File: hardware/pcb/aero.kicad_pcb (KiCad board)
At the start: 4 copper layers, 41 x 50 mm, 310 parts, among them CON1 USB-MICRO-B, CON2 MMCX_CONN, J1 CORTEX_DBG_CONN, J2 LiPoly_Conn, Q1 BSS138, SW1 SW_PUSH, U1 STM32L151C8, U10 BU4SU69G2, U11 BU4SU69G2, U12 NC7WZ17, U13 u-blox_max-7c/q, U14 MAX2659, U2 nRF8001, U3 2450BM14A0002, U4 ms5611, U5 BMX055, U6 AT45DB321E, U7 BQ24040DSQ, U8 TPS783, U9 TPS61041, Y1 Crystal, Y2 32.768KHz, Y3 16MHz

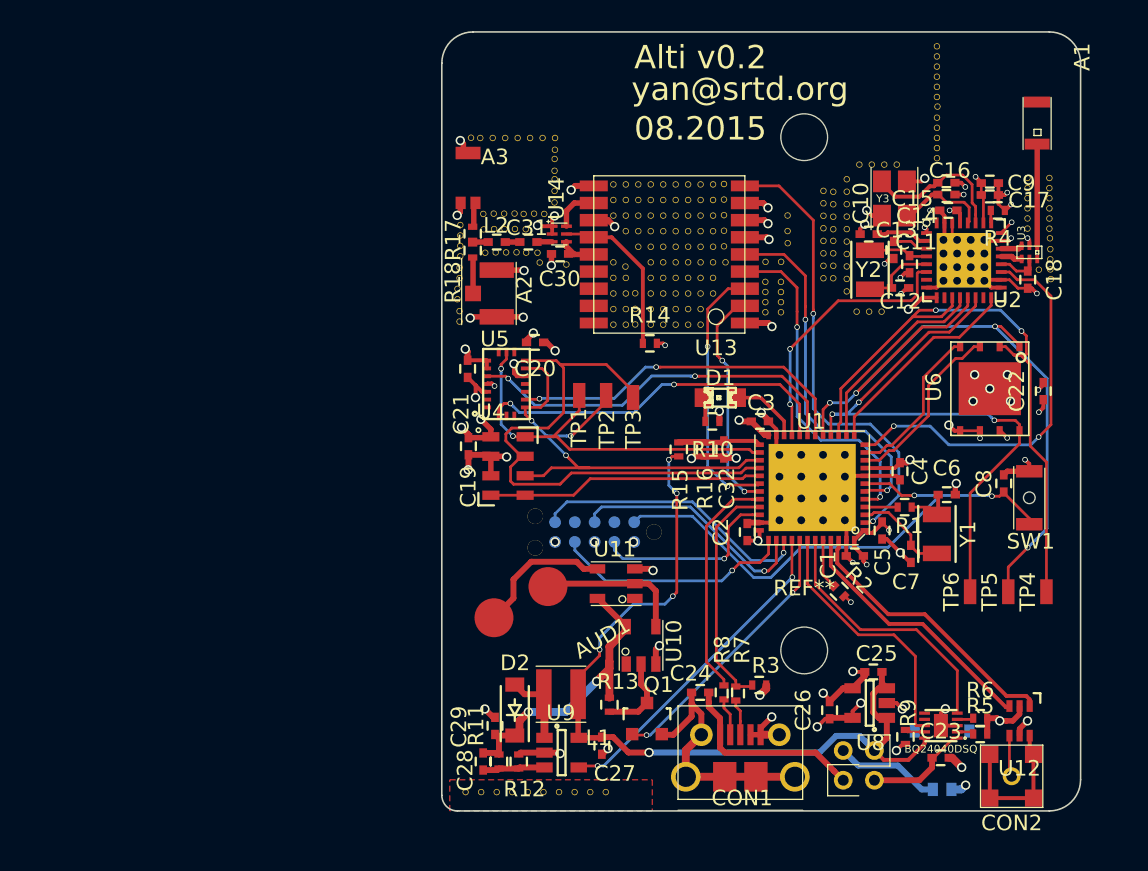
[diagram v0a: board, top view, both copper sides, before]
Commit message: moved balun further from nrf8001
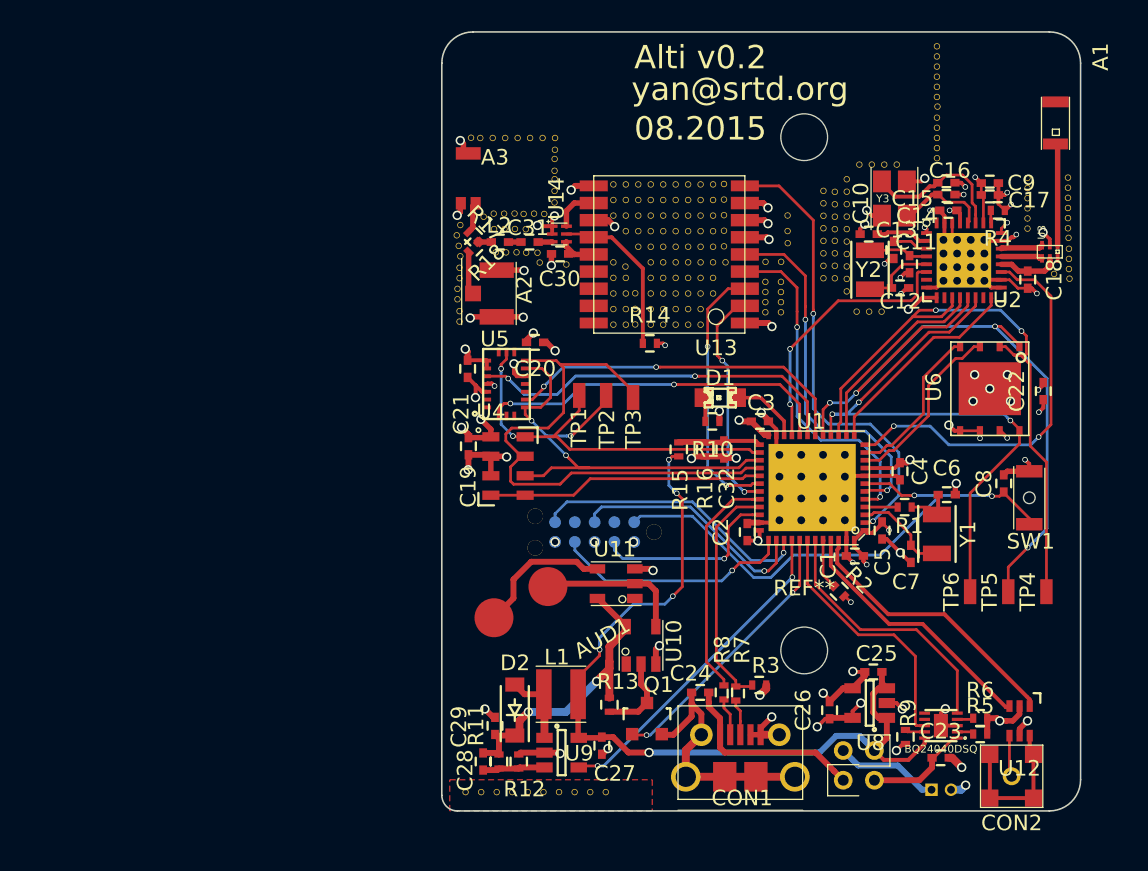
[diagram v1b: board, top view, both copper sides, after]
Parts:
- removed the REF**1111 at (127.8, 79.2)
- removed the REF**1111 at (127.7, 77.7)
- J2: footprint aero:Conn_Molex_78171-02 -> Connectors_Molex:Connector_Molex_PicoBlade_53048-0210
- moved U3 1.31 mm to (164.0, 79.1)
- moved REF**11611 1.19 mm to (165.2, 77.6)
- moved REF**11612 1.19 mm to (165.3, 79.6)
- moved REF**11613 1.19 mm to (165.3, 78.9)
- moved REF**11613 1.19 mm to (165.2, 76.3)
- moved REF**11615 1.19 mm to (165.2, 75.0)
- moved REF**11616 1.19 mm to (165.2, 74.4)
- moved REF**11611 1.19 mm to (165.3, 80.2)
- moved REF**11612 1.19 mm to (165.2, 77.0)
- moved REF**11614 1.19 mm to (165.2, 75.7)
- moved REF**11616 1.19 mm to (165.3, 80.8)
- moved REF**11616 1.19 mm to (165.2, 78.2)
- moved A1 1.18 mm to (164.4, 70.8)
- moved REF**11611 1.01 mm to (164.3, 80.5)
- moved J2 0.68 mm to (156.4, 113.6)
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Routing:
- net Net-(C18-Pad1): track 2.70 -> 4.07 mm
- net Net-(U2-Pad22): track 1.38 -> 2.71 mm
- net Net-(U2-Pad21): track 1.37 -> 2.66 mm
- net GND: track 126.0 -> 126.9 mm
- net /bmx055/GYRO_SEL: track 25.0 -> 24.4 mm

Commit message: Intermediate commit
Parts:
- moved A1 0.38 mm to (164.0, 70.8)
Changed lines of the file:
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@@
   )
   (setup
-    (last_trace_width 0.352298)
+    (last_trace_width 0.25)
     (user_trace_width 0.1524)
     (user_trace_width 0.1778)
@@
   )
   (module aero:2450AT18A100 (layer F.Cu)
-    (at 164.3888 70.8406 90)
-    (fp_text reference A1 (at 4.25 2.9 90) (layer F.SilkS)
+    (at 164.0078 70.8406 90)
+    (fp_text reference A1 (at 0.127 0.0254 90) (layer F.SilkS)
       (effects (font (size 1 1) (thickness 0.15)))
     )
@@
   (module aero:CONMMCX002-SMD (layer F.Cu)
     (at 161.576 112.776 270)
-    (fp_text reference CON2 (at 3 0 360) (layer F.SilkS)
+    (fp_text reference CON2 (at -0.1651 -2.5842 450) (layer F.SilkS)
       (effects (font (size 1 1) (thickness 0.15)))
     )
@@
     (tags SC-70-6,)
     (attr smd)
-    (fp_text reference U12 (at 0.01016 -3.05054 180) (layer F.SilkS)
+    (fp_text reference U12 (at -1.7333 0.1143 270) (layer F.SilkS)
       (effects (font (size 1 1) (thickness 0.15)))
     )

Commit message: pre-net import
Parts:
- removed A3: U.FL_Antenna, aero:Chip_Antenna_W3011A
- removed C30: 33nF, Capacitors_SMD:C_0402
- removed C31: 470pF, Capacitors_SMD:C_0402
- removed JP1, JP2: JUMPER, aero:Pin_Header_1x02_2mm
- removed L2: 6.8nH, Capacitors_SMD:C_0402
- removed R14: 10k, Resistors_SMD:R_0402
- removed R17, R18: 0, Resistors_SMD:R_0402
- removed the REF** at (148.3, 71.8)
- removed the REF** at (148.3, 104.7)
- removed REF**11101, REF**11102, REF**11103, REF**11104, REF**11105, REF**11106, REF**1111 (x33), REF**11110, REF**111101, REF**11111, REF**1112, REF**11121, REF**1113, REF**11131, REF**11141, REF**11151, REF**1116, REF**11161, REF**1117, REF**11171, REF**1118, REF**11181, REF**1119, REF**11191, REF**1121 (x3), REF**11210, REF**1122, REF**1123, REF**1124, REF**1126, REF**1127, REF**1128, REF**1129, REF**1131 (x2), REF**11310, REF**1132, REF**1133, REF**1134, REF**1135, REF**1138, REF**1139, REF**1141 (x2), REF**11410, REF**1142, REF**1143, REF**1144, REF**1145, REF**1146, REF**1147, REF**1148, REF**1149, REF**1151 (x2), REF**11510, REF**1152, REF**1153, REF**1154, REF**1155, REF**1156, REF**1157, REF**1158, REF**1159, REF**1161 (x2), REF**11610, REF**11611 (x5), REF**11612 (x5), REF**11613 (x5), REF**11614 (x4), REF**11615 (x4), REF**11616 (x7), REF**1162, REF**1163, REF**1164, REF**1165, REF**1166, REF**1167, REF**1168, REF**1169, REF**1171 (x2), REF**11710, REF**11711, REF**117111, REF**117112, REF**117113, REF**117114, REF**1172 (x2), REF**11721, REF**117211, REF**117212, REF**117213, REF**117214, REF**1173 (x2), REF**117311111 (x3), REF**1173111110, REF**117311112 (x3), REF**117311113 (x3), REF**117311114 (x2), REF**117311115 (x5), REF**117311116 (x5), REF**117311117 (x5), REF**117311118 (x5), REF**117311119, REF**1174 (x2), REF**1175, REF**1176, REF**1177, REF**1178, REF**1179, REF**1181 (x4), REF**11810, REF**1182, REF**1183, REF**1184, REF**1185, REF**1186, REF**1187, REF**1188, REF**1189, REF**1191, REF**1192, REF**1193, REF**1194, REF**1195, REF**1196, REF**1197, REF**1198: v, aero:Via_Stitch
- added P1: CONN_01X03, Pin_Headers:Pin_Header_Straight_1x03, F.Cu at (135.5, 95.8)
- added REF**: v, aero:Via_Stitch, F.Cu at (143.2, 101.2)
- added REF**: v, aero:Via_Stitch, F.Cu at (158.9, 96.7)
- added REF**: v, aero:Via_Stitch, F.Cu at (141.5, 102.5)
- added REF**: MountingHole_2-5mm, Mounting_Holes:MountingHole_2-5mm, F.Cu at (157.0, 68.0)
- added REF**: MountingHole_2-5mm, Mounting_Holes:MountingHole_2-5mm, F.Cu at (163.0, 112.3)
- added REF**: MountingHole_2-5mm, Mounting_Holes:MountingHole_2-5mm, F.Cu at (127.5, 112.2)
- added REF**: v, aero:Via_Stitch, F.Cu at (158.9, 95.8)
- added REF**: v, aero:Via_Stitch, F.Cu at (159.4, 84.7)
- A2: footprint aero:U.FL -> aero:CGGP.25.4.A.02; moved to B.Cu
- AUD1: moved to B.Cu
- J2: footprint Connectors_Molex:Connector_Molex_PicoBlade_53048-0210 -> Pin_Headers:Pin_Header_Straight_1x02; moved to F.Cu
- U14: value MAX2659 -> NC7WZ17; footprint aero:6-µDFN -> Housings_SOT-23_SOT-143_TSOT-6:SC-70-6
- moved CON2 35.2 mm to (127.4, 104.5), turned to 180 degrees
- moved U12 30.9 mm to (131.5, 105.0), turned to 90 degrees
- moved J1 28.0 mm to (162.8, 96.1), turned to 270 degrees
- moved C28 27.9 mm to (155.1, 106.6), turned to 90 degrees
- moved AUD1 27.6 mm to (157.5, 104.9), turned to 330 degrees
- moved C29 25.9 mm to (154.3, 108.9), turned to 270 degrees
- moved R11 25.9 mm to (154.0, 106.6), turned to 90 degrees
- moved R6 25.5 mm to (134.1, 108.2), turned to 90 degrees
- moved R5 24.5 mm to (135.1, 108.2), turned to 90 degrees
- moved U14 24.4 mm to (131.5, 102.3), turned to 90 degrees
- moved R12 23.4 mm to (152.8, 106.6), turned to 270 degrees
- moved D2 23.4 mm to (153.0, 110.5), turned to 270 degrees
- moved U7 22.5 mm to (134.6, 110.8), turned to 180 degrees
- moved C25 21.9 mm to (131.6, 111.9)
- moved R13 21.3 mm to (157.0, 109.7)
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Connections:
- net NRF8001_ENABLE renamed NRF8001_ACTIVE
- A1 pad 2: Net-(A1-Pad2) -> (no net)
- C24 pad 1: Net-(C24-Pad1) -> Net-(C23-Pad1)
- CON1 pad 1: Net-(C24-Pad1) -> Net-(C23-Pad1)
- J1 pad 9: Net-(J1-Pad9) -> (no net)
- J2 pad 1: Net-(J2-Pad1) -> Vbatt
- U1 pad 10: /at45db321e/~RESET -> /at45db321e/~CS
- U1 pad 11: /at45db321e/~CS -> /at45db321e/~RESET
- U1 pad 40: /warn/PIEZO_EN -> ~CHG
- U1 pad 41: /warn/PIEZO_OUT -> ~PG
- U1 pad 42: ~CHG -> /warn/WARN_LED_A
- U1 pad 43: ~PG -> /warn/WARN_LED_B
- U1 pad 45: /warn/WARN_LED_A -> /warn/PIEZO_EN
- U1 pad 46: /warn/WARN_LED_B -> /warn/PIEZO_OUT
- U10 pad 1: Net-(U10-Pad1) -> (no net)
- U11 pad 1: Net-(U11-Pad1) -> (no net)
- U13 pad 11: Net-(U13-Pad11) -> Net-(A2-Pad1)
- U13 pad 13: Net-(R14-Pad1) -> (no net)
- U13 pad 14: Net-(C30-Pad1) -> (no net)
- U13 pad 15: Net-(U13-Pad15) -> (no net)
- U13 pad 16: /GPS/SDA -> (no net)
- U13 pad 17: /GPS/SCL -> (no net)
- U13 pad 18: Net-(U13-Pad18) -> (no net)
- U14 pad 1: GND -> /warn/WARN_LED_B
- U14 pad 3: Net-(C31-Pad1) -> /warn/WARN_LED_A
- U14 pad 4: Net-(C30-Pad1) -> Net-(CON2-Pad1)
- U14 pad 5: Net-(R14-Pad1) -> +3V
- U14 pad 6: Net-(U13-Pad11) -> Net-(CON2-Pad2)
- U2 pad 10: /nRF8001/RXD -> (no net)
- U2 pad 15: Net-(U2-Pad15) -> (no net)
- U2 pad 32: Net-(U2-Pad32) -> (no net)
- U2 pad 7: /nRF8001/TXD -> (no net)
- U3 pad 6: Net-(U3-Pad6) -> (no net)
- U5 pad 1: Net-(U5-Pad1) -> (no net)
- U5 pad 10: Net-(U5-Pad10) -> (no net)
- U5 pad 14: Net-(U5-Pad14) -> (no net)
- U5 pad 15: Net-(U5-Pad15) -> (no net)
- U5 pad 18: Net-(U5-Pad18) -> (no net)
- U5 pad 19: /bmx055/ACC_INT -> (no net)
- U5 pad 2: Net-(U5-Pad2) -> (no net)
- U5 pad 8: Net-(U5-Pad8) -> (no net)
- U6 pad : GND -> (no net)
- U7 pad 6: Net-(U7-Pad6) -> (no net)
- U7 pad 7: Net-(U7-Pad7) -> (no net)
- Y3 pad 3: GND -> (no net)
- Y3 pad 4: GND -> (no net)
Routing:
- net GPS_RX: track 17.6 -> 60.2 mm, vias 2 -> 1
- net GPS_TX: track 14.7 -> 57.2 mm, vias 2 -> 1
- net /GPS/EXT_INT: track 23.9 -> 50.6 mm
- net GND: track 126.9 -> 104.1 mm, vias 63 -> 49
- net /GPS/RESET: track 29.8 -> 51.6 mm
- net /GPS/TIMEPULSE: track 21.9 -> 43.2 mm, vias 2 -> 3
- net Net-(J1-Pad2): track 12.3 -> 29.9 mm
- net /at45db321e/SCK: track 40.5 -> 25.6 mm
- net Net-(C24-Pad1): track 12.6 -> 0.00 mm
- net /warn/PIEZO_EN: track 21.2 -> 9.24 mm, vias 2 -> 0
- net Net-(J1-Pad4): track 15.4 -> 27.2 mm
- net /warn/STATUS_LED: track 4.56 -> 15.8 mm, vias 0 -> 2
- net ~CHG: track 16.7 -> 27.7 mm, vias 0 -> 2
- net Net-(R14-Pad1): track 10.8 -> 0.00 mm
- net /at45db321e/MOSI: track 46.5 -> 36.1 mm, vias 4 -> 3
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- added copper zone on B.Cu, net GND
- removed copper zone on F.Cu, net GND
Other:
- board text added: "10.2015"
- board text added: "Alti v0.3"
- board text added: "RX"
- board text added: "TX"
- board text removed: "08.2015"
- board text removed: "Alti v0.2"

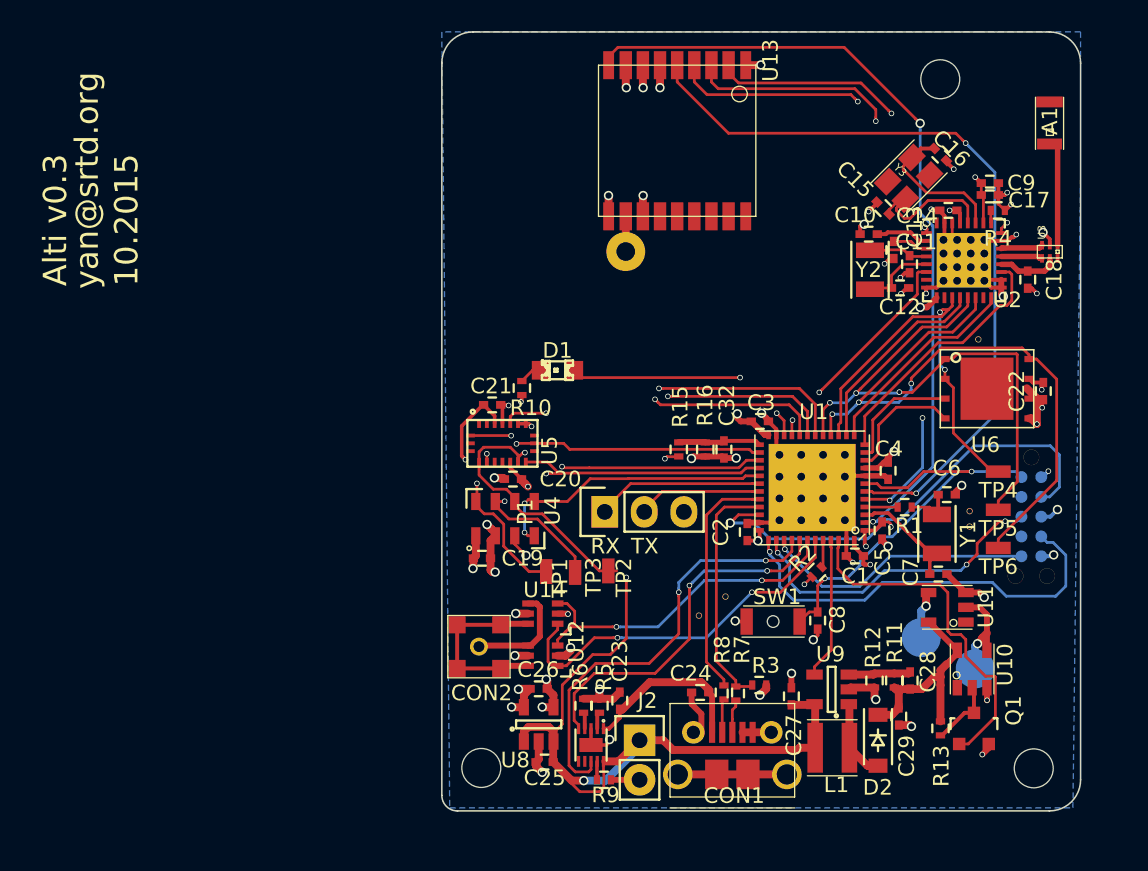
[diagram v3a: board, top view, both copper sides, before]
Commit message: passes DRC with stitching
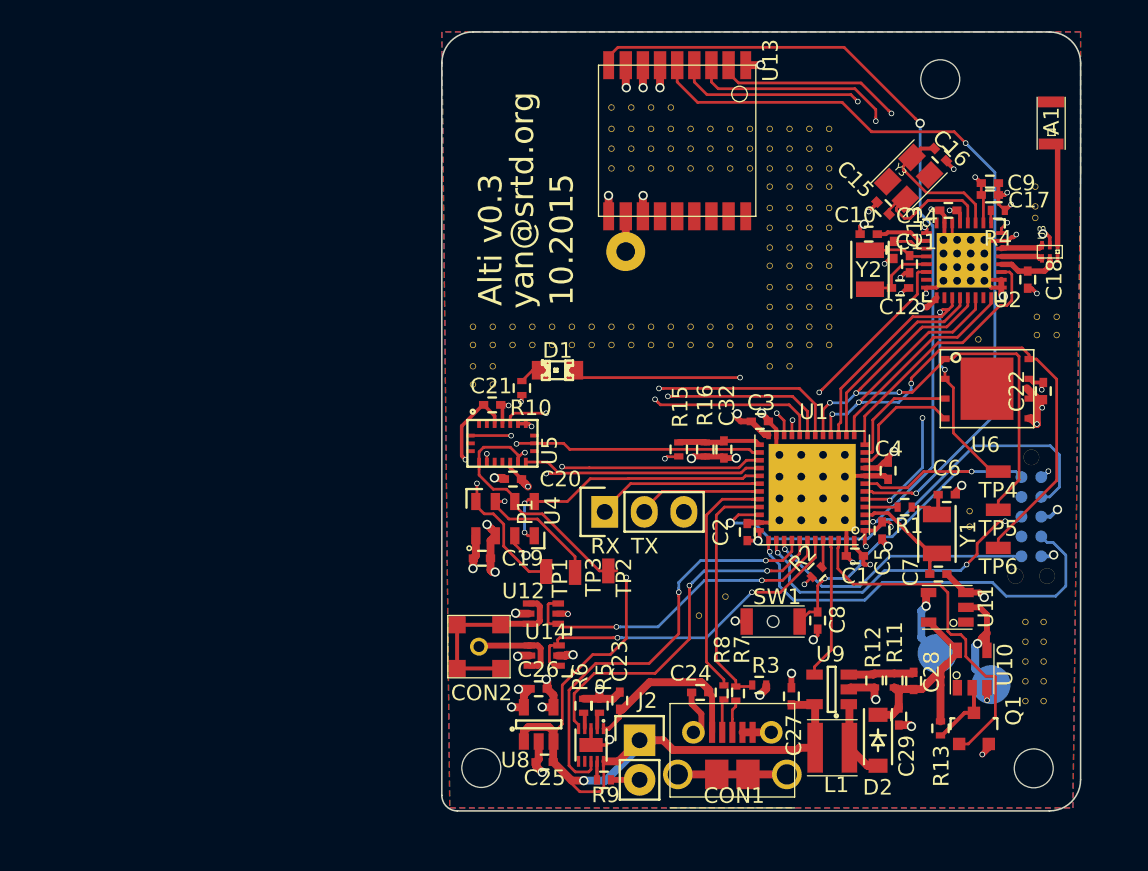
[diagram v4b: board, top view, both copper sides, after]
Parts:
- added REF**: v, aero:Via_Stitch, F.Cu at (127.0, 87.6)
- added REF**: v, aero:Via_Stitch, F.Cu at (129.5, 83.9)
- added REF**: v, aero:Via_Stitch, F.Cu at (148.6, 71.2)
- added REF**: v, aero:Via_Stitch, F.Cu at (148.6, 72.5)
- added REF**: v, aero:Via_Stitch, F.Cu at (141.0, 73.8)
- added REF**: v, aero:Via_Stitch, F.Cu at (142.2, 73.8)
- added REF**: v, aero:Via_Stitch, F.Cu at (143.5, 73.8)
- added REF**: v, aero:Via_Stitch, F.Cu at (144.8, 73.8)
- added REF**: v, aero:Via_Stitch, F.Cu at (142.2, 71.2)
- added REF**: v, aero:Via_Stitch, F.Cu at (141.0, 71.2)
- added REF**: v, aero:Via_Stitch, F.Cu at (144.8, 72.5)
- added REF**: v, aero:Via_Stitch, F.Cu at (144.8, 71.2)
- added REF**: v, aero:Via_Stitch, F.Cu at (163.1, 76.9)
- added REF**: v, aero:Via_Stitch, F.Cu at (141.0, 72.5)
- added REF**: v, aero:Via_Stitch, F.Cu at (142.2, 72.5)
- added REF**: v, aero:Via_Stitch, F.Cu at (143.5, 71.2)
- added REF**: v, aero:Via_Stitch, F.Cu at (143.5, 72.5)
- added REF**: v, aero:Via_Stitch, F.Cu at (139.7, 69.8)
- added REF**: v, aero:Via_Stitch, F.Cu at (139.7, 71.2)
- added REF**: v, aero:Via_Stitch, F.Cu at (139.7, 72.5)
- added REF**: v, aero:Via_Stitch, F.Cu at (139.7, 73.8)
- added REF**: v, aero:Via_Stitch, F.Cu at (138.4, 69.8)
- added REF**: v, aero:Via_Stitch, F.Cu at (138.4, 71.2)
- added REF**: v, aero:Via_Stitch, F.Cu at (163.1, 74.9)
- added REF**: v, aero:Via_Stitch, F.Cu at (138.4, 72.5)
- added REF**: v, aero:Via_Stitch, F.Cu at (138.4, 73.8)
- added REF**: v, aero:Via_Stitch, F.Cu at (137.2, 69.8)
- added REF**: v, aero:Via_Stitch, F.Cu at (137.2, 71.2)
- added REF**: v, aero:Via_Stitch, F.Cu at (137.2, 72.5)
- added REF**: v, aero:Via_Stitch, F.Cu at (137.2, 73.8)
- added REF**: v, aero:Via_Stitch, F.Cu at (135.9, 73.8)
- added REF**: v, aero:Via_Stitch, F.Cu at (135.9, 72.5)
- added REF**: v, aero:Via_Stitch, F.Cu at (135.9, 71.2)
- added REF**: v, aero:Via_Stitch, F.Cu at (163.1, 76.2)
- added REF**: v, aero:Via_Stitch, F.Cu at (135.9, 69.8)
- added REF**: v, aero:Via_Stitch, F.Cu at (163.2, 83.3)
- added REF**: v, aero:Via_Stitch, F.Cu at (163.2, 84.5)
- added REF**: v, aero:Via_Stitch, F.Cu at (164.5, 84.5)
- added REF**: v, aero:Via_Stitch, F.Cu at (164.5, 83.3)
- added REF**: v, aero:Via_Stitch, F.Cu at (163.6, 102.9)
- added REF**: v, aero:Via_Stitch, F.Cu at (162.5, 102.9)
- added REF**: v, aero:Via_Stitch, F.Cu at (128.3, 87.6)
- added REF**: v, aero:Via_Stitch, F.Cu at (163.6, 104.1)
- added REF**: v, aero:Via_Stitch, F.Cu at (162.5, 104.1)
- added REF**: v, aero:Via_Stitch, F.Cu at (162.5, 105.4)
- added REF**: v, aero:Via_Stitch, F.Cu at (163.6, 105.4)
- added REF**: v, aero:Via_Stitch, F.Cu at (162.5, 106.7)
- added REF**: v, aero:Via_Stitch, F.Cu at (162.5, 108.0)
- added REF**: v, aero:Via_Stitch, F.Cu at (163.6, 106.7)
- added REF**: v, aero:Via_Stitch, F.Cu at (163.6, 108.0)
- added REF**: v, aero:Via_Stitch, F.Cu at (143.5, 85.1)
- added REF**: v, aero:Via_Stitch, F.Cu at (144.8, 85.1)
- added REF**: v, aero:Via_Stitch, F.Cu at (127.0, 86.5)
- added REF**: v, aero:Via_Stitch, F.Cu at (144.8, 83.9)
- added REF**: v, aero:Via_Stitch, F.Cu at (143.5, 83.9)
- added REF**: v, aero:Via_Stitch, F.Cu at (142.2, 85.1)
- added REF**: v, aero:Via_Stitch, F.Cu at (141.0, 85.1)
- added REF**: v, aero:Via_Stitch, F.Cu at (142.2, 83.9)
- added REF**: v, aero:Via_Stitch, F.Cu at (141.0, 83.9)
- added REF**: v, aero:Via_Stitch, F.Cu at (138.4, 85.1)
- added REF**: v, aero:Via_Stitch, F.Cu at (139.7, 85.1)
- added REF**: v, aero:Via_Stitch, F.Cu at (139.7, 83.9)
- added REF**: v, aero:Via_Stitch, F.Cu at (138.4, 83.9)
- added REF**: v, aero:Via_Stitch, F.Cu at (128.3, 86.5)
- added REF**: v, aero:Via_Stitch, F.Cu at (137.2, 85.1)
- added REF**: v, aero:Via_Stitch, F.Cu at (135.9, 85.1)
- added REF**: v, aero:Via_Stitch, F.Cu at (137.2, 83.9)
- added REF**: v, aero:Via_Stitch, F.Cu at (135.9, 83.9)
- added REF**: v, aero:Via_Stitch, F.Cu at (133.3, 85.1)
- added REF**: v, aero:Via_Stitch, F.Cu at (134.6, 85.1)
- added REF**: v, aero:Via_Stitch, F.Cu at (134.6, 83.9)
- added REF**: v, aero:Via_Stitch, F.Cu at (133.3, 83.9)
- added REF**: v, aero:Via_Stitch, F.Cu at (132.1, 85.1)
- added REF**: v, aero:Via_Stitch, F.Cu at (130.8, 85.1)
- added REF**: v, aero:Via_Stitch, F.Cu at (127.0, 83.9)
- added REF**: v, aero:Via_Stitch, F.Cu at (132.1, 83.9)
- added REF**: v, aero:Via_Stitch, F.Cu at (130.8, 83.9)
- added REF**: v, aero:Via_Stitch, F.Cu at (147.3, 86.5)
- added REF**: v, aero:Via_Stitch, F.Cu at (147.3, 85.1)
- added REF**: v, aero:Via_Stitch, F.Cu at (146.1, 85.1)
- added REF**: v, aero:Via_Stitch, F.Cu at (146.1, 86.5)
- added REF**: v, aero:Via_Stitch, F.Cu at (149.9, 85.1)
- added REF**: v, aero:Via_Stitch, F.Cu at (148.6, 85.1)
- added REF**: v, aero:Via_Stitch, F.Cu at (146.1, 83.9)
- added REF**: v, aero:Via_Stitch, F.Cu at (147.3, 83.9)
- added REF**: v, aero:Via_Stitch, F.Cu at (127.0, 85.1)
- added REF**: v, aero:Via_Stitch, F.Cu at (148.6, 83.9)
- added REF**: v, aero:Via_Stitch, F.Cu at (149.9, 83.9)
- added REF**: v, aero:Via_Stitch, F.Cu at (147.3, 81.4)
- added REF**: v, aero:Via_Stitch, F.Cu at (147.3, 80.0)
- added REF**: v, aero:Via_Stitch, F.Cu at (146.1, 80.0)
- added REF**: v, aero:Via_Stitch, F.Cu at (146.1, 81.4)
- added REF**: v, aero:Via_Stitch, F.Cu at (149.9, 82.7)
- added REF**: v, aero:Via_Stitch, F.Cu at (149.9, 80.0)
- added REF**: v, aero:Via_Stitch, F.Cu at (148.6, 80.0)
- added REF**: v, aero:Via_Stitch, F.Cu at (149.9, 81.4)
- added REF**: v, aero:Via_Stitch, F.Cu at (128.3, 85.1)
- added REF**: v, aero:Via_Stitch, F.Cu at (146.1, 82.7)
- added REF**: v, aero:Via_Stitch, F.Cu at (147.3, 82.7)
- added REF**: v, aero:Via_Stitch, F.Cu at (148.6, 81.4)
- added REF**: v, aero:Via_Stitch, F.Cu at (148.6, 82.7)
- added REF**: v, aero:Via_Stitch, F.Cu at (146.1, 78.8)
- added REF**: v, aero:Via_Stitch, F.Cu at (147.3, 78.8)
- added REF**: v, aero:Via_Stitch, F.Cu at (148.6, 78.8)
- added REF**: v, aero:Via_Stitch, F.Cu at (149.9, 78.8)
- added REF**: v, aero:Via_Stitch, F.Cu at (147.3, 76.3)
- added REF**: v, aero:Via_Stitch, F.Cu at (147.3, 74.9)
- added REF**: v, aero:Via_Stitch, F.Cu at (128.3, 83.9)
- added REF**: v, aero:Via_Stitch, F.Cu at (146.1, 74.9)
- added REF**: v, aero:Via_Stitch, F.Cu at (146.1, 76.3)
- added REF**: v, aero:Via_Stitch, F.Cu at (149.9, 77.6)
- added REF**: v, aero:Via_Stitch, F.Cu at (149.9, 74.9)
- added REF**: v, aero:Via_Stitch, F.Cu at (148.6, 74.9)
- added REF**: v, aero:Via_Stitch, F.Cu at (149.9, 76.3)
- added REF**: v, aero:Via_Stitch, F.Cu at (146.1, 77.6)
- added REF**: v, aero:Via_Stitch, F.Cu at (147.3, 77.6)
- added REF**: v, aero:Via_Stitch, F.Cu at (148.6, 76.3)
- added REF**: v, aero:Via_Stitch, F.Cu at (148.6, 77.6)
- added REF**: v, aero:Via_Stitch, F.Cu at (129.5, 85.1)
- added REF**: v, aero:Via_Stitch, F.Cu at (146.1, 73.8)
- added REF**: v, aero:Via_Stitch, F.Cu at (147.3, 73.8)
- added REF**: v, aero:Via_Stitch, F.Cu at (148.6, 73.8)
- added REF**: v, aero:Via_Stitch, F.Cu at (149.9, 73.8)
- added REF**: v, aero:Via_Stitch, F.Cu at (147.3, 71.2)
- added REF**: v, aero:Via_Stitch, F.Cu at (146.1, 71.2)
- added REF**: v, aero:Via_Stitch, F.Cu at (149.9, 72.5)
- added REF**: v, aero:Via_Stitch, F.Cu at (149.9, 71.2)
- added REF**: v, aero:Via_Stitch, F.Cu at (146.1, 72.5)
- added REF**: v, aero:Via_Stitch, F.Cu at (147.3, 72.5)
- moved U12 2.70 mm to (131.5, 102.3)
- moved U14 2.69 mm to (131.6, 105.0)
- moved AUD1 1.44 mm to (158.5, 105.9)
- moved C28 0.23 mm to (155.3, 106.7)
- moved A1 0.10 mm to (164.1, 70.8)
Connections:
- U12 pad 1: /warn/WARN_LED_B -> /warn/WARN_LED_A
- U12 pad 4: Net-(CON2-Pad1) -> Net-(CON2-Pad2)
- U14 pad 3: /warn/WARN_LED_A -> /warn/WARN_LED_B
- U14 pad 6: Net-(CON2-Pad2) -> Net-(CON2-Pad1)
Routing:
- net Net-(AUD1-Pad2): track 6.43 -> 7.87 mm, vias 1 -> 2
- net Net-(AUD1-Pad1): track 3.09 -> 4.52 mm
- net /warn/WARN_LED_B: track 24.0 -> 22.6 mm
- net Net-(CON2-Pad1): track 7.13 -> 6.09 mm
- net Net-(CON2-Pad2): track 12.3 -> 13.3 mm
- net /warn/WARN_LED_A: track 22.2 -> 21.5 mm
- net /GPS/RESET: track 51.6 -> 51.1 mm
- net GND: track 104.1 -> 104.0 mm, vias 49 -> 48
- added copper zone on F.Cu, net GND
